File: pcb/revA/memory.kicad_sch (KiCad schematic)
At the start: 2 parts, among them U12 CY62167EV30LL

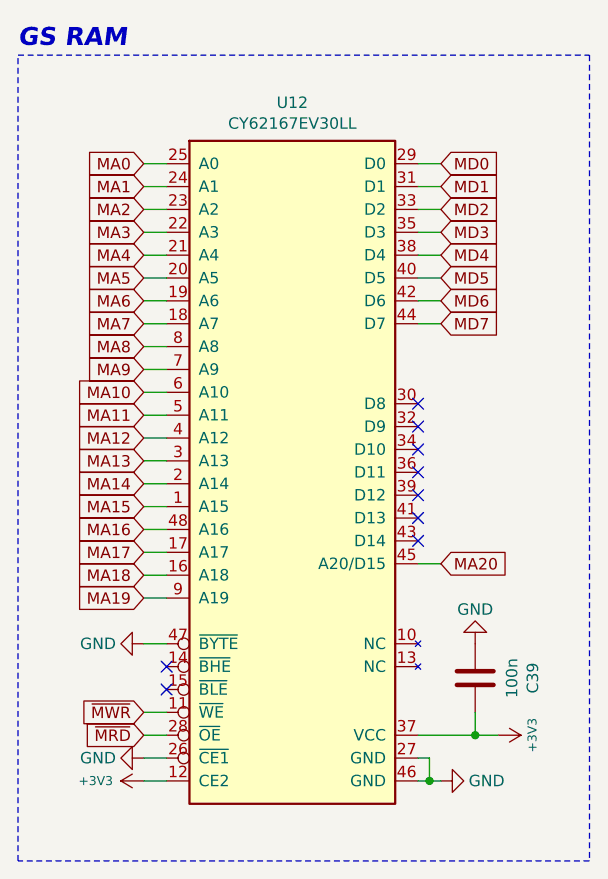
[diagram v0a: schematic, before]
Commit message: Updated gerbers to min 0.2/0.45 vias, firmware build for xc6slx16
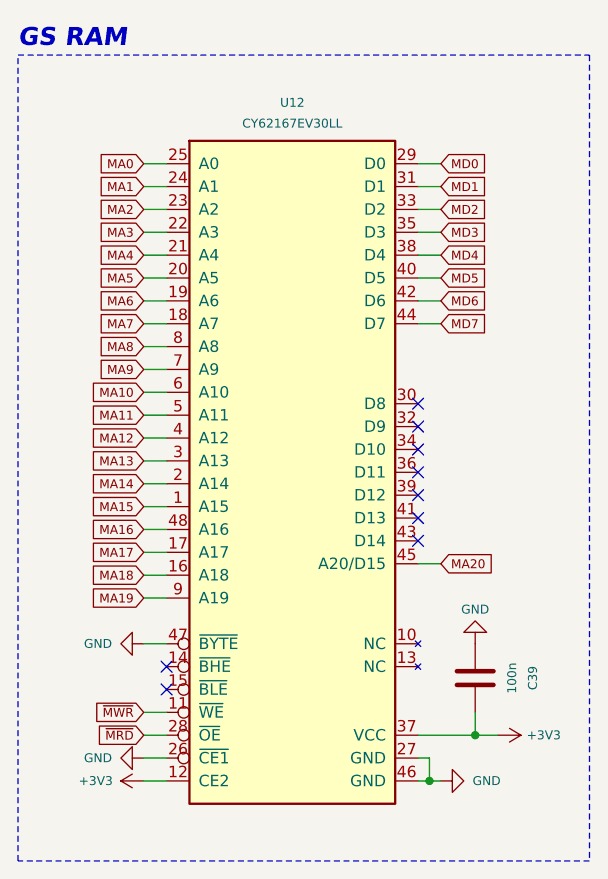
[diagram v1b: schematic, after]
